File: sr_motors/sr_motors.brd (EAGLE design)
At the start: 78.4 x 64.8 mm, 20 parts

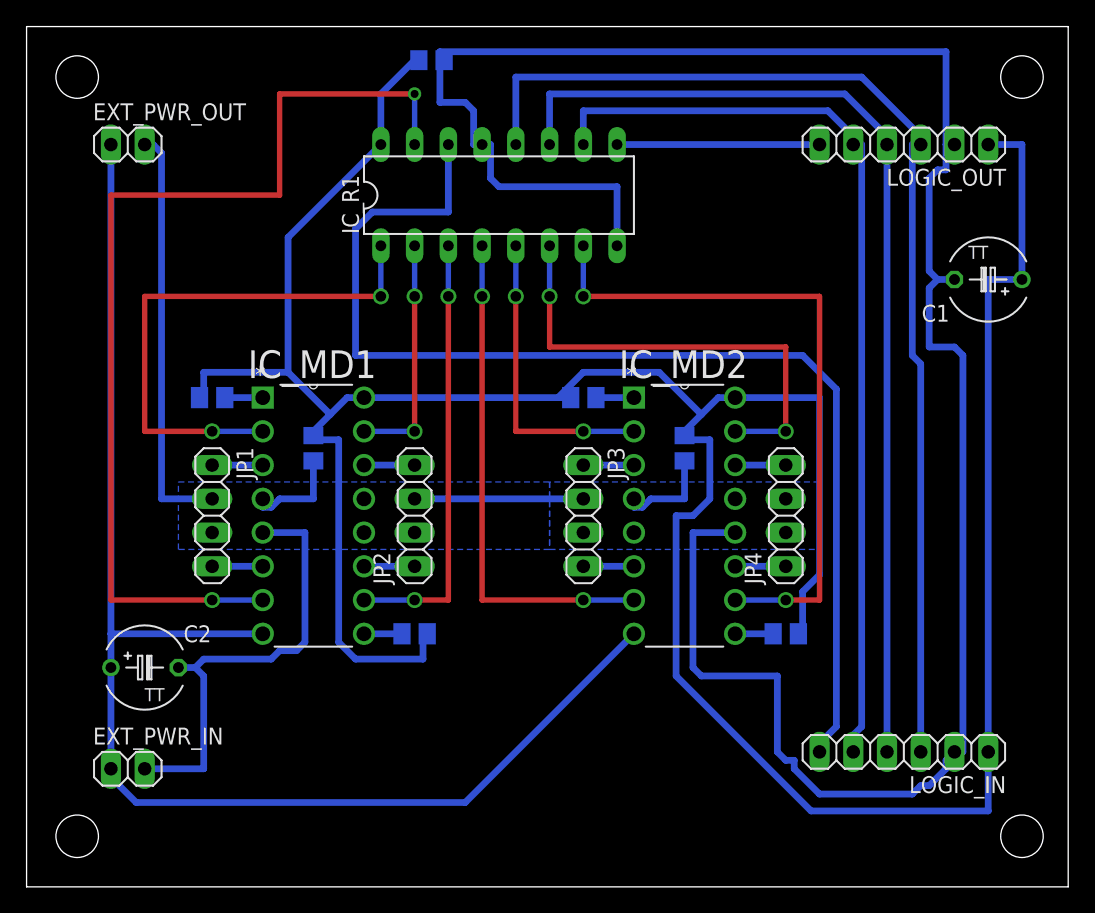
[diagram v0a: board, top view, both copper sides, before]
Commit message: Route rework: - increased distance between wires - shifted capacitors, connectors and IC's - rerouted EN signals - other small changes
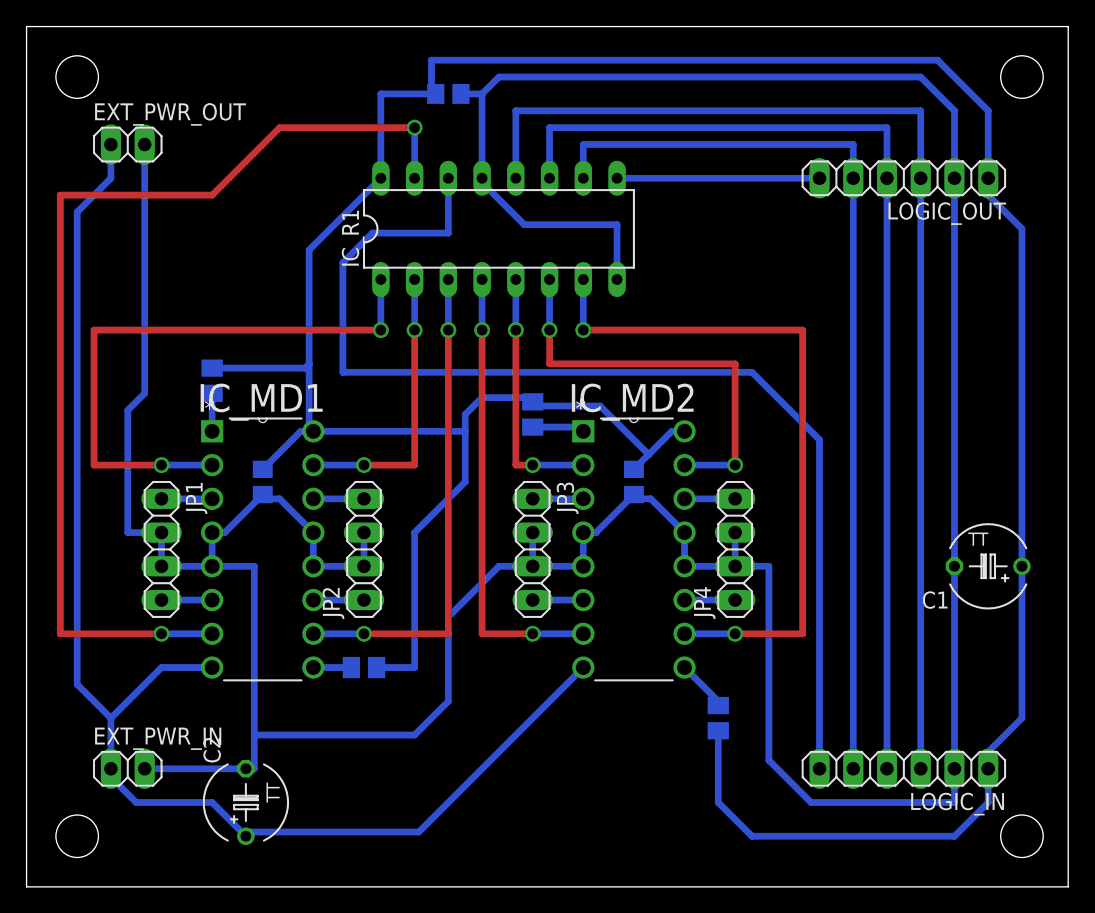
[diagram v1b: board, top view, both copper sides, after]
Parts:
- moved C1 21.6 mm to (72.4, 24.1)
- moved C2 12.7 mm to (16.5, 6.35), turned to 90 degrees
- moved R14 8.13 mm to (52.1, 12.7), turned to 270 degrees
- moved C5 4.58 mm to (45.7, 30.5)
- moved JP2 4.58 mm to (25.4, 25.4)
- moved IC_MD2 4.58 mm to (49.5, 16.5)
- moved JP1 4.58 mm to (10.2, 25.4)
- moved R2 4.58 mm to (25.4, 16.5)
- moved C4 4.58 mm to (17.8, 30.5)
- moved IC_MD1 4.58 mm to (21.6, 16.5)
- moved JP3 4.58 mm to (38.1, 25.4)
- moved JP4 4.58 mm to (53.3, 25.4)
- moved R1 4.02 mm to (38.1, 35.6), turned to 90 degrees
- moved C3 2.84 mm to (31.8, 59.7)
- moved IC_R1 2.54 mm to (35.6, 49.5)
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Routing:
- net GND: track 260.1 -> 290.3 mm
- net VCC1: track 235.9 -> 227.9 mm
- net Q5: track 22.9 -> 19.0 mm
- net Q4: track 38.1 -> 34.3 mm
- net Q3: track 33.0 -> 36.8 mm
- net Q1: track 40.6 -> 44.5 mm
- net Q2: track 17.8 -> 21.6 mm
- net Q6: track 35.6 -> 31.8 mm
- net SI0: track 87.2 -> 84.0 mm
- net VCC2: track 104.5 -> 101.8 mm
- net Q7: track 50.8 -> 52.1 mm
- net EN2: track 2.86 -> 3.94 mm
- net SCLR: track 70.9 -> 69.8 mm
- net EN3: track 2.86 -> 3.91 mm
- net Q0: track 76.2 -> 77.0 mm
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- removed copper zone on layer 16, net GND
